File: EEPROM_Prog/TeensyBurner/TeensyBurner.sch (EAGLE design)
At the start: 10 parts, among them IC1 74LS595N, IC2 74LS595N, J1 POWER_JACK

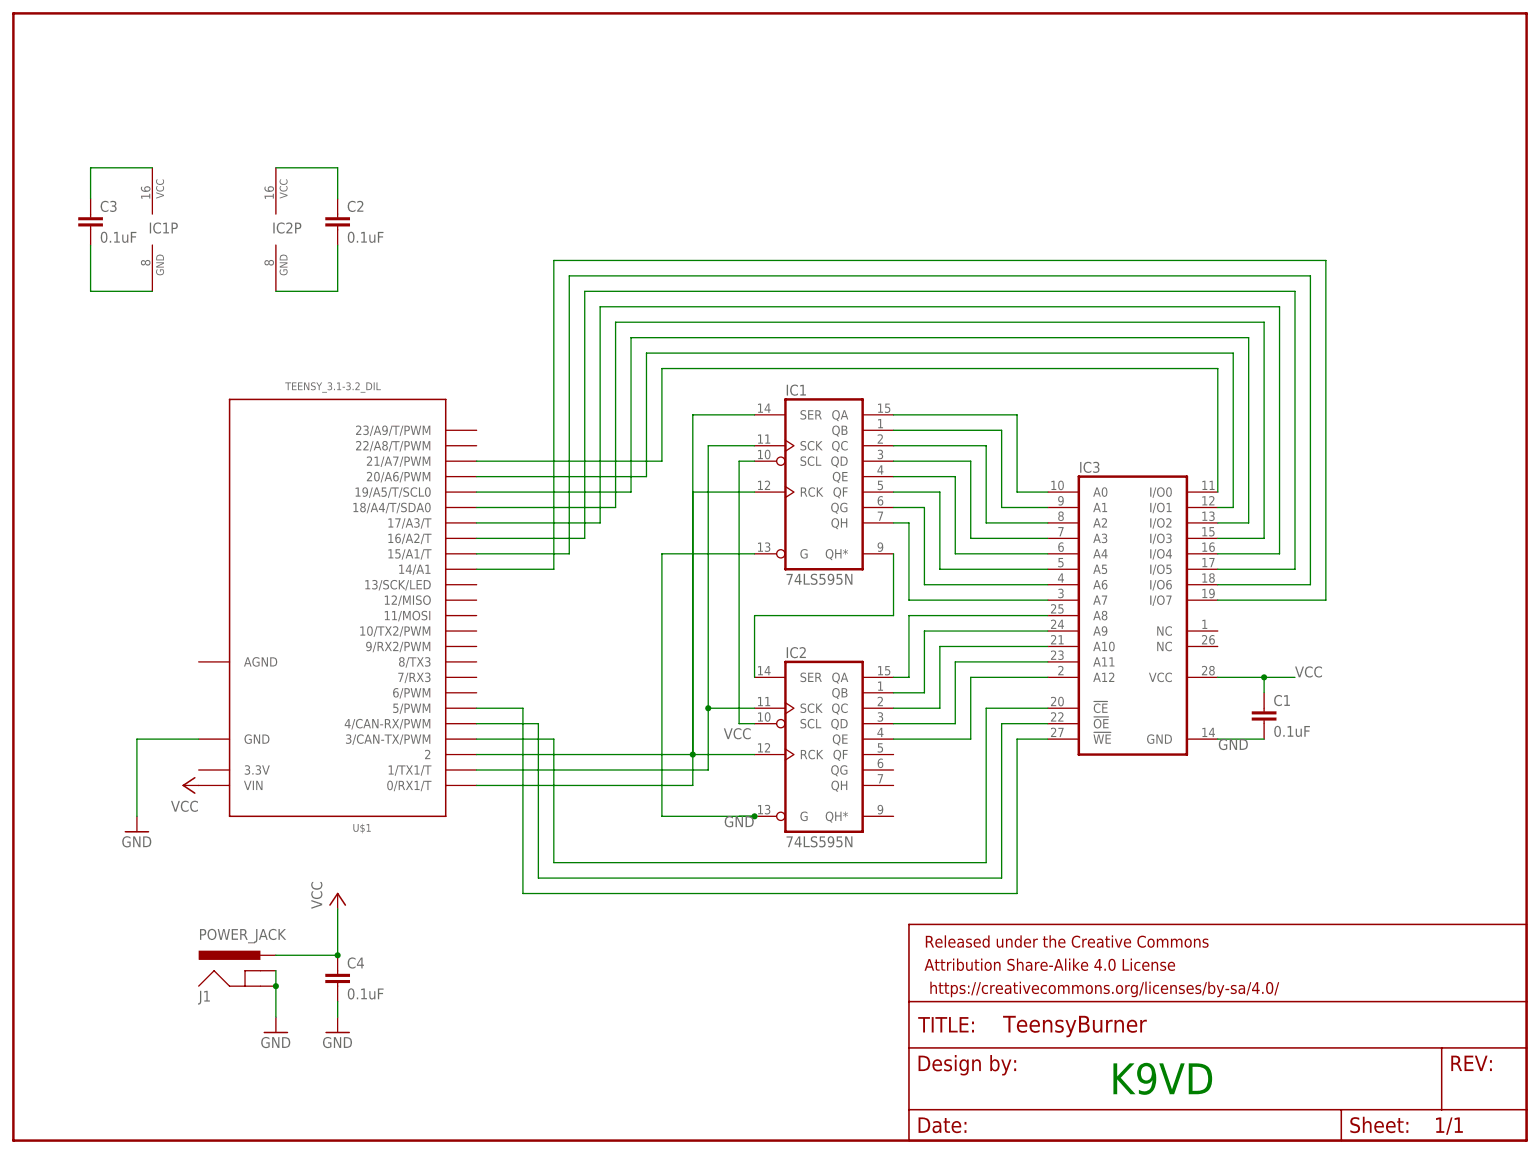
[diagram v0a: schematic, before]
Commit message: Updated Eagle files
Upladed an old version, this corrected that.
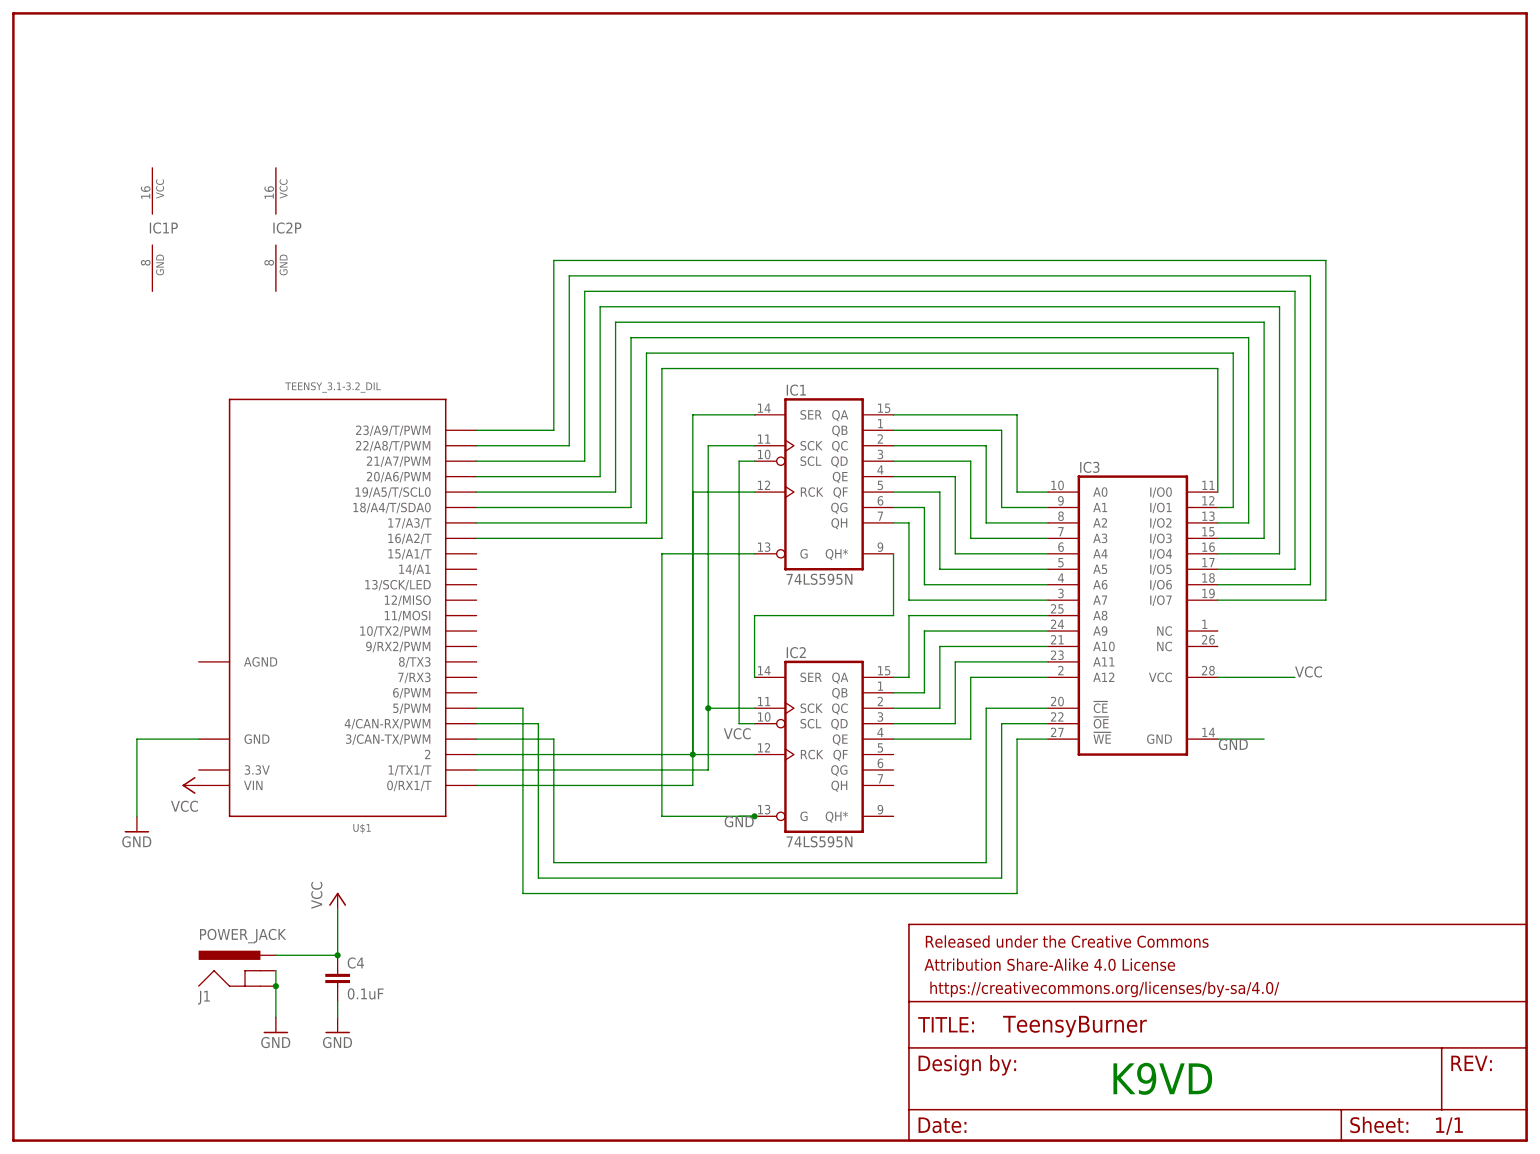
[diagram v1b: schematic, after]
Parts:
- removed C1, C2, C3: 0.1uF, SparkFun-Capacitors:0.1UF-KIT-EZ-50V-20%
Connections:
- removed net N$25: IC3.I/O7, U$1.14/A1
- new net N$36: IC3.I/O7, U$1.23/A9/T/PWM
- net GND: no longer C1.2, C2.2, C3.2, IC1P.GND, IC2P.GND
- net N$18: now also U$1.16/A2/T; no longer U$1.21/A7/PWM
- net N$19: now also U$1.17/A3/T; no longer U$1.20/A6/PWM
- net N$20: now also U$1.18/A4/T/SDA0; no longer U$1.19/A5/T/SCL0
- net N$21: now also U$1.19/A5/T/SCL0; no longer U$1.18/A4/T/SDA0
- net N$22: now also U$1.20/A6/PWM; no longer U$1.17/A3/T
- net N$23: now also U$1.21/A7/PWM; no longer U$1.16/A2/T
- net N$24: now also U$1.22/A8/T/PWM; no longer U$1.15/A1/T
- net VCC: no longer C1.1, C2.1, C3.1, IC1P.VCC, IC2P.VCC
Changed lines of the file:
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@@
 <part name="P+1" library="supply1" deviceset="VCC" device=""/>
 <part name="GND1" library="supply1" deviceset="GND" device=""/>
-<part name="C1" library="SparkFun-Capacitors" deviceset="0.1UF" device="-KIT-EZ-50V-20%" value="0.1uF"/>
-<part name="C2" library="SparkFun-Capacitors" deviceset="0.1UF" device="-KIT-EZ-50V-20%" value="0.1uF"/>
-<part name="C3" library="SparkFun-Capacitors" deviceset="0.1UF" device="-KIT-EZ-50V-20%" value="0.1uF"/>
 <part name="J1" library="SparkFun-Connectors" deviceset="POWER_JACK" device=""/>
 <part name="VCC" library="supply1" deviceset="VCC" device=""/>
@@
 <instance part="P+1" gate="VCC" x="27.94" y="58.42" rot="R90"/>
 <instance part="GND1" gate="1" x="20.32" y="50.8"/>
-<instance part="C1" gate="G$1" x="205.74" y="68.58"/>
 <instance part="IC1" gate="P" x="22.86" y="149.86"/>
 <instance part="IC2" gate="P" x="43.18" y="149.86"/>
-<instance part="C2" gate="G$1" x="53.34" y="149.86"/>
-<instance part="C3" gate="G$1" x="12.7" y="149.86"/>
 <instance part="J1" gate="G$1" x="40.64" y="22.86"/>
 <instance part="VCC" gate="VCC" x="53.34" y="40.64"/>
@@
 <net name="N$18" class="0">
 <segment>
-<pinref part="U$1" gate="G$1" pin="21/A7/PWM"/>
-<wire x1="76.2" y1="111.76" x2="106.68" y2="111.76" width="0.1524" layer="91"/>
-<wire x1="106.68" y1="111.76" x2="106.68" y2="127" width="0.1524" layer="91"/>
 <pinref part="IC3" gate="G$1" pin="I/O0"/>
 <wire x1="106.68" y1="127" x2="198.12" y2="127" width="0.1524" layer="91"/>
 <wire x1="198.12" y1="127" x2="198.12" y2="106.68" width="0.1524" layer="91"/>
+<pinref part="U$1" gate="G$1" pin="16/A2/T"/>
+<wire x1="76.2" y1="99.06" x2="106.68" y2="99.06" width="0.1524" layer="91"/>
+<wire x1="106.68" y1="99.06" x2="106.68" y2="127" width="0.1524" layer="91"/>
 </segment>
 </net>
 <net name="N$19" class="0">
 <segment>
-<pinref part="U$1" gate="G$1" pin="20/A6/PWM"/>
-<wire x1="76.2" y1="109.22" x2="104.14" y2="109.22" width="0.1524" layer="91"/>
-<wire x1="104.14" y1="109.22" x2="104.14" y2="129.54" width="0.1524" layer="91"/>
 <wire x1="104.14" y1="129.54" x2="200.66" y2="129.54" width="0.1524" layer="91"/>
 <wire x1="200.66" y1="129.54" x2="200.66" y2="104.14" width="0.1524" layer="91"/>
 <pinref part="IC3" gate="G$1" pin="I/O1"/>
 <wire x1="200.66" y1="104.14" x2="198.12" y2="104.14" width="0.1524" layer="91"/>
+<pinref part="U$1" gate="G$1" pin="17/A3/T"/>
+<wire x1="76.2" y1="101.6" x2="104.14" y2="101.6" width="0.1524" layer="91"/>
+<wire x1="104.14" y1="101.6" x2="104.14" y2="129.54" width="0.1524" layer="91"/>
 </segment>
 </net>
@@
 <wire x1="203.2" y1="101.6" x2="203.2" y2="132.08" width="0.1524" layer="91"/>
 <wire x1="203.2" y1="132.08" x2="101.6" y2="132.08" width="0.1524" layer="91"/>
-<wire x1="101.6" y1="132.08" x2="101.6" y2="106.68" width="0.1524" layer="91"/>
-<pinref part="U$1" gate="G$1" pin="19/A5/T/SCL0"/>
-<wire x1="101.6" y1="106.68" x2="76.2" y2="106.68" width="0.1524" layer="91"/>
+<pinref part="U$1" gate="G$1" pin="18/A4/T/SDA0"/>
+<wire x1="76.2" y1="104.14" x2="101.6" y2="104.14" width="0.1524" layer="91"/>
+<wire x1="101.6" y1="104.14" x2="101.6" y2="132.08" width="0.1524" layer="91"/>
 </segment>
 </net>
 <net name="N$21" class="0">
 <segment>
-<pinref part="U$1" gate="G$1" pin="18/A4/T/SDA0"/>
-<wire x1="76.2" y1="104.14" x2="99.06" y2="104.14" width="0.1524" layer="91"/>
-<wire x1="99.06" y1="104.14" x2="99.06" y2="134.62" width="0.1524" layer="91"/>
 <wire x1="99.06" y1="134.62" x2="205.74" y2="134.62" width="0.1524" layer="91"/>
 <wire x1="205.74" y1="134.62" x2="205.74" y2="99.06" width="0.1524" layer="91"/>
 <pinref part="IC3" gate="G$1" pin="I/O3"/>
 <wire x1="205.74" y1="99.06" x2="198.12" y2="99.06" width="0.1524" layer="91"/>
+<pinref part="U$1" gate="G$1" pin="19/A5/T/SCL0"/>
+<wire x1="76.2" y1="106.68" x2="99.06" y2="106.68" width="0.1524" layer="91"/>
+<wire x1="99.06" y1="106.68" x2="99.06" y2="134.62" width="0.1524" layer="91"/>
 </segment>
 </net>
@@
 <wire x1="208.28" y1="96.52" x2="208.28" y2="137.16" width="0.1524" layer="91"/>
 <wire x1="208.28" y1="137.16" x2="96.52" y2="137.16" width="0.1524" layer="91"/>
-<wire x1="96.52" y1="137.16" x2="96.52" y2="101.6" width="0.1524" layer="91"/>
-<pinref part="U$1" gate="G$1" pin="17/A3/T"/>
-<wire x1="96.52" y1="101.6" x2="76.2" y2="101.6" width="0.1524" layer="91"/>
+<pinref part="U$1" gate="G$1" pin="20/A6/PWM"/>
+<wire x1="76.2" y1="109.22" x2="96.52" y2="109.22" width="0.1524" layer="91"/>
+<wire x1="96.52" y1="109.22" x2="96.52" y2="137.16" width="0.1524" layer="91"/>
 </segment>
 </net>
 <net name="N$23" class="0">
 <segment>
-<pinref part="U$1" gate="G$1" pin="16/A2/T"/>
-<wire x1="76.2" y1="99.06" x2="93.98" y2="99.06" width="0.1524" layer="91"/>
-<wire x1="93.98" y1="99.06" x2="93.98" y2="139.7" width="0.1524" layer="91"/>
 <wire x1="93.98" y1="139.7" x2="210.82" y2="139.7" width="0.1524" layer="91"/>
 <wire x1="210.82" y1="139.7" x2="210.82" y2="93.98" width="0.1524" layer="91"/>
 <pinref part="IC3" gate="G$1" pin="I/O5"/>
 <wire x1="210.82" y1="93.98" x2="198.12" y2="93.98" width="0.1524" layer="91"/>
+<pinref part="U$1" gate="G$1" pin="21/A7/PWM"/>
+<wire x1="76.2" y1="111.76" x2="93.98" y2="111.76" width="0.1524" layer="91"/>
+<wire x1="93.98" y1="111.76" x2="93.98" y2="139.7" width="0.1524" layer="91"/>
 </segment>
 </net>
@@
 <wire x1="213.36" y1="91.44" x2="213.36" y2="142.24" width="0.1524" layer="91"/>
 <wire x1="213.36" y1="142.24" x2="91.44" y2="142.24" width="0.1524" layer="91"/>
-<wire x1="91.44" y1="142.24" x2="91.44" y2="96.52" width="0.1524" layer="91"/>
-<pinref part="U$1" gate="G$1" pin="15/A1/T"/>
-<wire x1="91.44" y1="96.52" x2="76.2" y2="96.52" width="0.1524" layer="91"/>
-</segment>
-</net>
-<net name="N$25" class="0">
-<segment>
-<pinref part="U$1" gate="G$1" pin="14/A1"/>
-<wire x1="76.2" y1="93.98" x2="88.9" y2="93.98" width="0.1524" layer="91"/>
-<wire x1="88.9" y1="93.98" x2="88.9" y2="144.78" width="0.1524" layer="91"/>
-<wire x1="88.9" y1="144.78" x2="215.9" y2="144.78" width="0.1524" layer="91"/>
-<wire x1="215.9" y1="144.78" x2="215.9" y2="88.9" width="0.1524" layer="91"/>
-<pinref part="IC3" gate="G$1" pin="I/O7"/>
-<wire x1="215.9" y1="88.9" x2="198.12" y2="88.9" width="0.1524" layer="91"/>
+<pinref part="U$1" gate="G$1" pin="22/A8/T/PWM"/>
+<wire x1="76.2" y1="114.3" x2="91.44" y2="114.3" width="0.1524" layer="91"/>
+<wire x1="91.44" y1="114.3" x2="91.44" y2="142.24" width="0.1524" layer="91"/>
 </segment>
 </net>
@@
 <segment>
 <pinref part="IC3" gate="G$1" pin="GND"/>
-<pinref part="C1" gate="G$1" pin="2"/>
 <wire x1="198.12" y1="66.04" x2="205.74" y2="66.04" width="0.1524" layer="91"/>
 <label x="203.2" y="66.04" size="1.778" layer="95" rot="R180"/>
@@
 <wire x1="53.34" y1="22.86" x2="53.34" y2="20.32" width="0.1524" layer="91"/>
 </segment>
-<segment>
-<pinref part="C2" gate="G$1" pin="2"/>
-<wire x1="53.34" y1="147.32" x2="53.34" y2="139.7" width="0.1524" layer="91"/>
-<pinref part="IC2" gate="P" pin="GND"/>
-<wire x1="53.34" y1="139.7" x2="43.18" y2="139.7" width="0.1524" layer="91"/>
-</segment>
-<segment>
-<pinref part="C3" gate="G$1" pin="2"/>
-<wire x1="12.7" y1="147.32" x2="12.7" y2="139.7" width="0.1524" layer="91"/>
-<pinref part="IC1" gate="P" pin="GND"/>
-<wire x1="12.7" y1="139.7" x2="22.86" y2="139.7" width="0.1524" layer="91"/>
-</segment>
 </net>
 <net name="VCC" class="0">
@@
 <segment>
 <pinref part="IC3" gate="G$1" pin="VCC"/>
-<wire x1="198.12" y1="76.2" x2="205.74" y2="76.2" width="0.1524" layer="91"/>
-<pinref part="C1" gate="G$1" pin="1"/>
-<wire x1="205.74" y1="76.2" x2="205.74" y2="73.66" width="0.1524" layer="91"/>
-<junction x="205.74" y="76.2"/>
-<wire x1="205.74" y1="76.2" x2="210.82" y2="76.2" width="0.1524" layer="91"/>
+<wire x1="198.12" y1="76.2" x2="210.82" y2="76.2" width="0.1524" layer="91"/>
 <label x="210.82" y="76.2" size="1.778" layer="95"/>
 </segment>
@@
 <pinref part="C4" gate="G$1" pin="1"/>
 <junction x="53.34" y="30.48"/>
-</segment>
-<segment>
-<pinref part="IC1" gate="P" pin="VCC"/>
-<wire x1="22.86" y1="160.02" x2="12.7" y2="160.02" width="0.1524" layer="91"/>
-<pinref part="C3" gate="G$1" pin="1"/>
-<wire x1="12.7" y1="160.02" x2="12.7" y2="154.94" width="0.1524" layer="91"/>
-</segment>
-<segment>
-<pinref part="IC2" gate="P" pin="VCC"/>
-<wire x1="43.18" y1="160.02" x2="53.34" y2="160.02" width="0.1524" layer="91"/>
-<pinref part="C2" gate="G$1" pin="1"/>
-<wire x1="53.34" y1="160.02" x2="53.34" y2="154.94" width="0.1524" layer="91"/>
 </segment>
 </net>
@@
 </segment>
 </net>
+<net name="N$36" class="0">
+<segment>
+<pinref part="U$1" gate="G$1" pin="23/A9/T/PWM"/>
+<wire x1="76.2" y1="116.84" x2="88.9" y2="116.84" width="0.1524" layer="91"/>
+<wire x1="88.9" y1="144.78" x2="215.9" y2="144.78" width="0.1524" layer="91"/>
+<wire x1="215.9" y1="144.78" x2="215.9" y2="88.9" width="0.1524" layer="91"/>
+<pinref part="IC3" gate="G$1" pin="I/O7"/>
+<wire x1="215.9" y1="88.9" x2="198.12" y2="88.9" width="0.1524" layer="91"/>
+<wire x1="88.9" y1="116.84" x2="88.9" y2="144.78" width="0.1524" layer="91"/>
+</segment>
+</net>
